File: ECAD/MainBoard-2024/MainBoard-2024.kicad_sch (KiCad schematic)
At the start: 67 parts, among them J1 XT60, J10 Conn_01x14, J11 Conn_01x03, J12 Conn_01x04, J13 Conn_01x03, J14 Conn_01x03, J16 XT30, J17 XT30, J2 Conn_01x04, J20 BAU, J21 BAU, J22 Conn_01x04, J23 Conn_01x02, J26 BAU, J27 BAU, J28 Conn_01x02, J29 Conn_01x02, J3 ConStep1, J30 Conn_01x03, J5 ConStep1, J6 ConStep1, J7 XT30, J8 Conn_01x02, J9 XT60, K1 CB1-P-24V, U1 Teensy3.5_All_Pins, U2 R-78B3.3-2.0, U3 PCA9685PW, U4 R-78B5.0-2.0

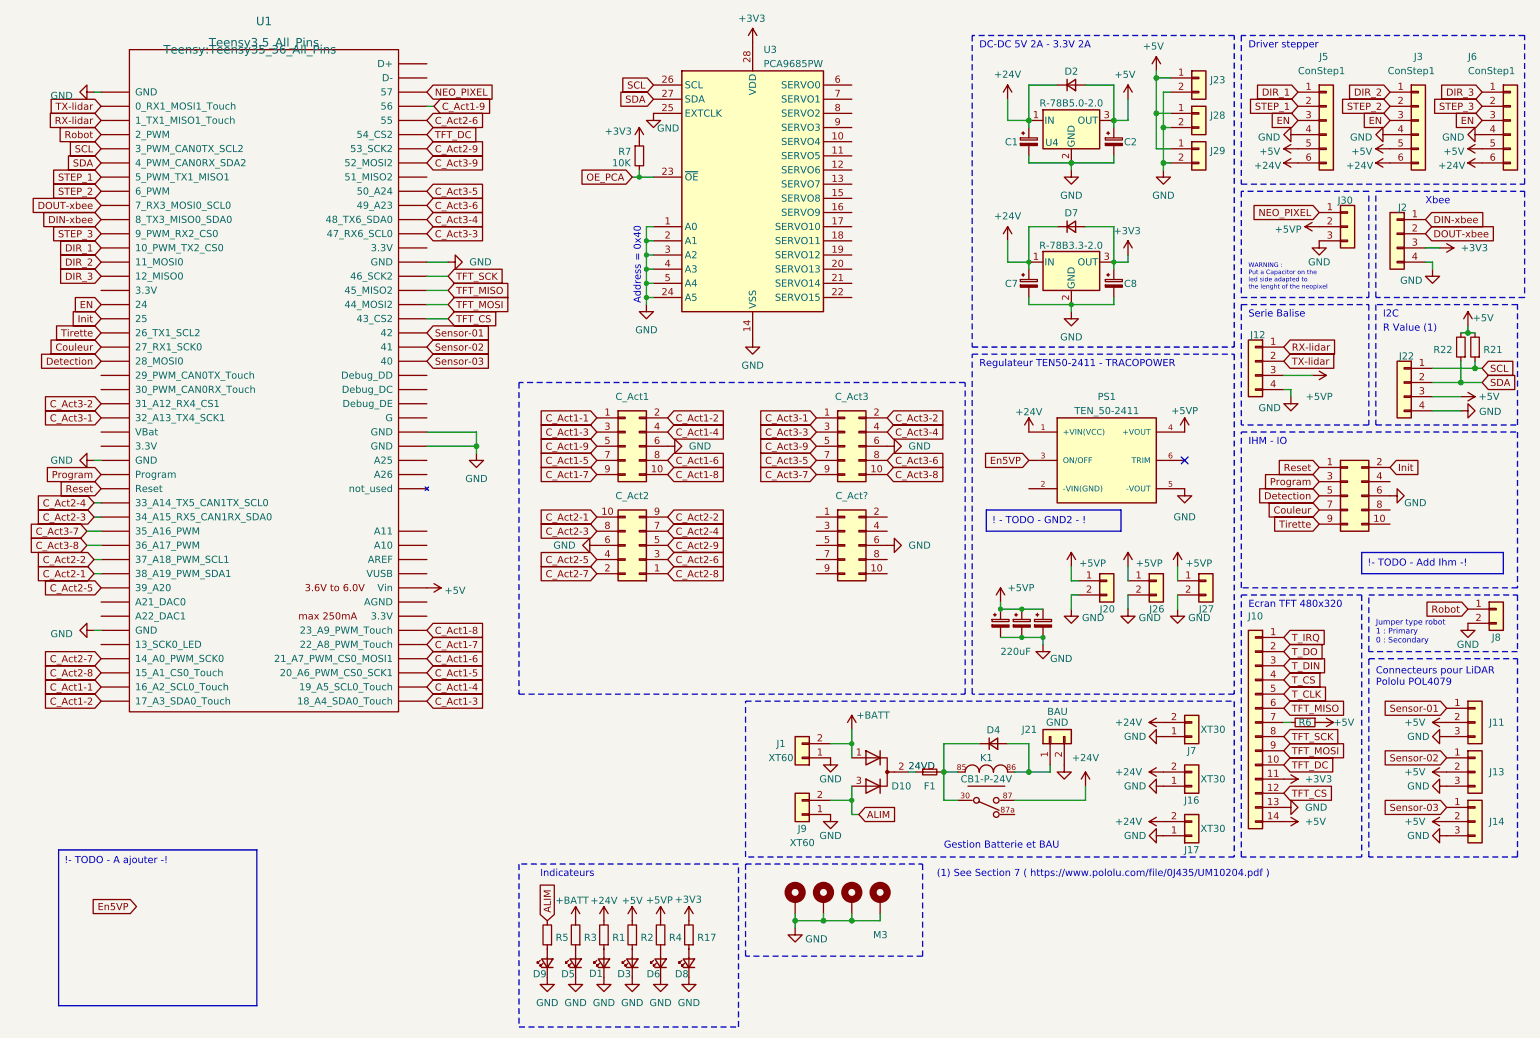
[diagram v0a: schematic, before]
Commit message: update component and edge cut
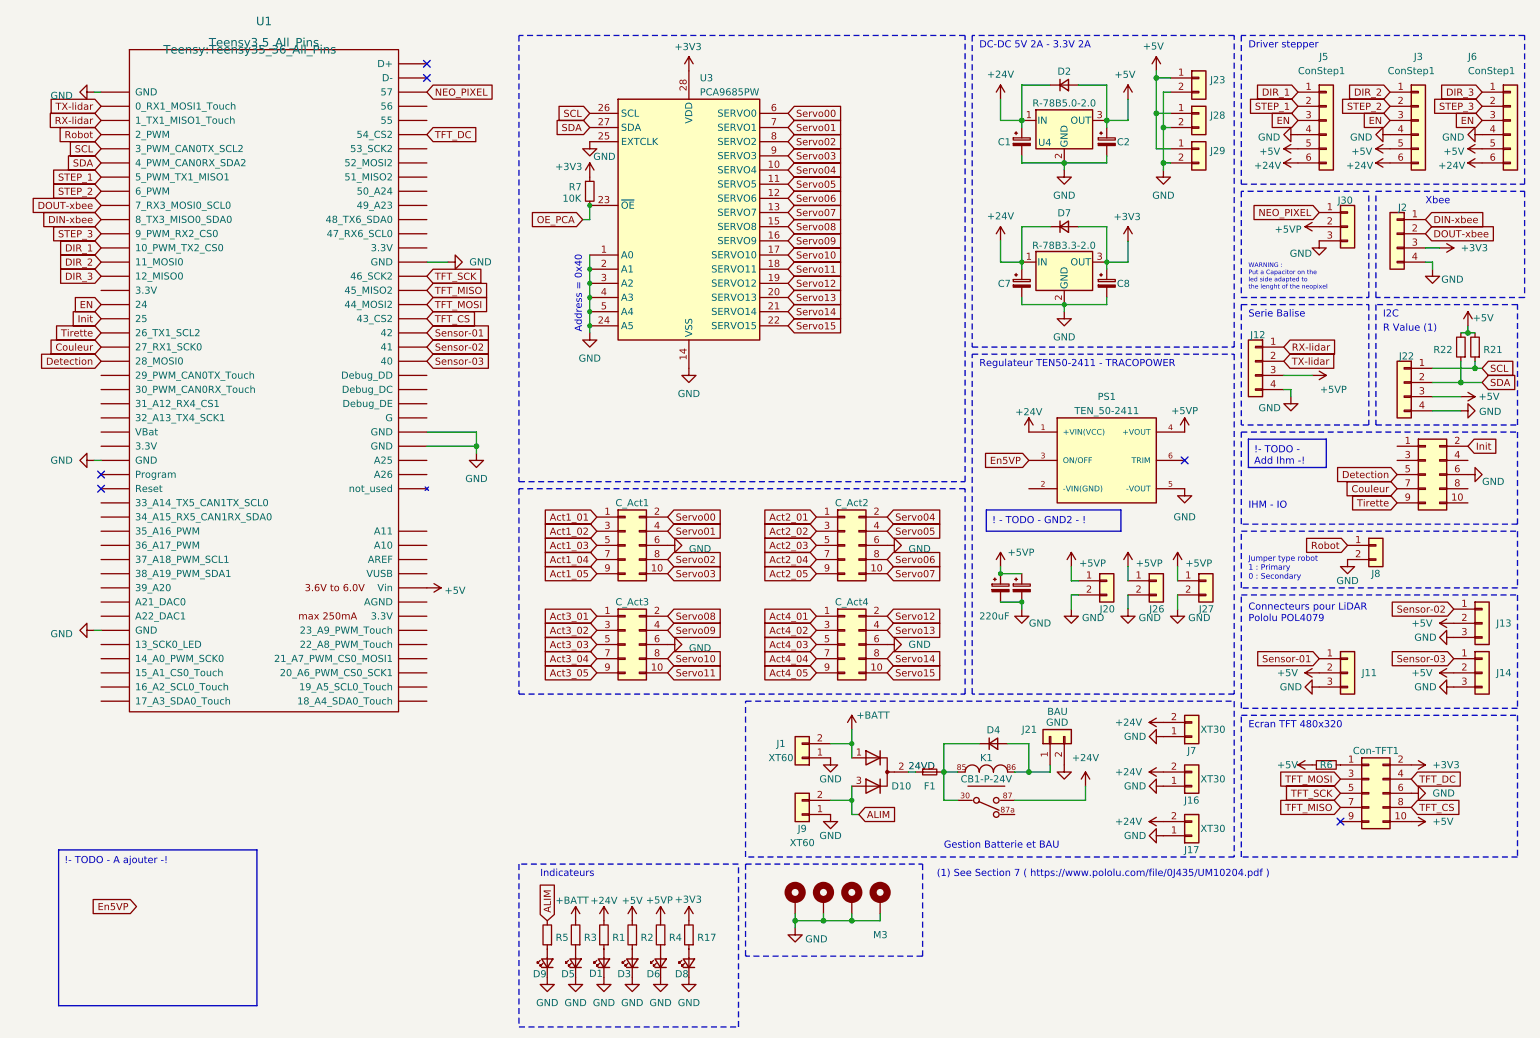
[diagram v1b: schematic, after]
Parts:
- removed C3: 220uF, Capacitor_THT:CP_Radial_D8.0mm_P3.80mm, symbol Device:CP_Small
- removed J10: Conn_01x14, Connector_PinSocket_2.54mm:PinSocket_1x14_P2.54mm_Vertical, symbol Connector_Generic:Conn_01x14
- added Con-TFT1: Conn_02x05_Odd_Even, Connector_IDC:IDC-Header_2x05_P2.54mm_Vertical, symbol Connector_Generic:Conn_02x05_Odd_Even
- gave numbers to parts that had none: 1
- renumbered C_Act3 to C_Act2, C_Act2 to C_Act3, C_Act4 to IHM-IO1
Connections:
- net +3V3: now also Con-TFT1.2 (Pin_2)
- net +5V: now also Con-TFT1.10 (Pin_10)
- net GND: now also Con-TFT1.6 (Pin_6)
- net TFT_CS: now also Con-TFT1.8 (Pin_8)
- net TFT_DC: now also Con-TFT1.4 (Pin_4)
- net TFT_MISO: now also Con-TFT1.7 (Pin_7)
- net TFT_MOSI: now also Con-TFT1.3 (Pin_3)
- net TFT_SCK: now also Con-TFT1.5 (Pin_5)
- net Servo04: now reaches U3.10 (SERVO4)
- net Servo04: now also C_Act2.2 (Pin_2)
- net Servo05: now reaches U3.11 (SERVO5)
- net Servo05: now also C_Act2.4 (Pin_4)
- net Servo06: now reaches U3.12 (SERVO6)
- net Servo06: now also C_Act2.8 (Pin_8)
- net Servo07: now reaches U3.13 (SERVO7)
- net Servo07: now also C_Act2.10 (Pin_10)
- net Servo08: now reaches U3.15 (SERVO8)
- net Servo08: now also C_Act3.2 (Pin_2)
- net Servo09: now reaches U3.16 (SERVO9)
- net Servo09: now also C_Act3.4 (Pin_4)
- net Servo10: now reaches U3.17 (SERVO10)
- net Servo10: now also C_Act3.8 (Pin_8)
- net Servo11: now reaches U3.18 (SERVO11)
- net Servo11: now also C_Act3.10 (Pin_10)
- net Servo12: now reaches U3.19 (SERVO12)
- net Servo12: now also C_Act4.2 (Pin_2)
- net Servo13: now reaches U3.20 (SERVO13)
- net Servo13: now also C_Act4.4 (Pin_4)
- net Servo14: now reaches U3.21 (SERVO14)
- net Servo14: now also C_Act4.8 (Pin_8)
- net Servo15: now reaches U3.22 (SERVO15)
- net Servo15: now also C_Act4.10 (Pin_10)
- net Servo00: now reaches U3.6 (SERVO0)
- net Servo00: now also C_Act1.2 (Pin_2)
- net Servo01: now reaches U3.7 (SERVO1)
- net Servo01: now also C_Act1.4 (Pin_4)
- net Servo02: now reaches U3.8 (SERVO2)
- net Servo02: now also C_Act1.8 (Pin_8)
- net Servo03: now reaches U3.9 (SERVO3)
- net Servo03: now also C_Act1.10 (Pin_10)
- net Act4_01: now reaches C_Act4.1 (Pin_1)
- net Act4_02: now reaches C_Act4.3 (Pin_3)
- net Act4_03: now reaches C_Act4.5 (Pin_5)
- net Act4_04: now reaches C_Act4.7 (Pin_7)
- net Act4_05: now reaches C_Act4.9 (Pin_9)
- net at R6.2: now also Con-TFT1.1 (Pin_1)
- net C_Act1-1: no longer names the net of U1.43 (16_A2_SCL0_Touch)
- net C_Act1-1: no longer C_Act1.1 (Pin_1)
- net C_Act1-2: no longer names the net of U1.44 (17_A3_SDA0_Touch)
- net C_Act1-2: no longer C_Act1.2 (Pin_2)
- net C_Act1-3: no longer names the net of U1.45 (18_A4_SDA0_Touch)
- net C_Act1-3: no longer C_Act1.3 (Pin_3)
- net C_Act1-4: no longer names the net of U1.46 (19_A5_SCL0_Touch)
- net C_Act1-4: no longer C_Act1.4 (Pin_4)
- net C_Act1-5: no longer names the net of U1.47 (20_A6_PWM_CS0_SCK1)
- net C_Act1-5: no longer C_Act1.7 (Pin_7)
- net C_Act1-6: no longer names the net of U1.48 (21_A7_PWM_CS0_MOSI1)
- net C_Act1-6: no longer C_Act1.8 (Pin_8)
- net C_Act1-7: no longer names the net of U1.49 (22_A8_PWM_Touch)
- net C_Act1-7: no longer C_Act1.9 (Pin_9)
- net C_Act1-8: no longer names the net of U1.50 (23_A9_PWM_Touch)
- net C_Act1-8: no longer C_Act1.10 (Pin_10)
- net C_Act1-9: no longer names the net of U1.85 (56)
- net C_Act1-9: no longer C_Act1.5 (Pin_5)
- net C_Act2-1: no longer names the net of U1.35 (38_A19_PWM_SDA1)
- net C_Act2-1: no longer C_Act3.10 (Pin_10)
- net C_Act2-2: no longer names the net of U1.34 (37_A18_PWM_SCL1)
- net C_Act2-2: no longer C_Act3.9 (Pin_9)
- net C_Act2-3: no longer names the net of U1.31 (34_A15_RX5_CAN1RX_SDA0)
- net C_Act2-3: no longer C_Act3.8 (Pin_8)
- net C_Act2-4: no longer names the net of U1.30 (33_A14_TX5_CAN1TX_SCL0)
- net C_Act2-4: no longer C_Act3.7 (Pin_7)
- net C_Act2-5: no longer names the net of U1.36 (39_A20)
- net C_Act2-5: no longer C_Act3.4 (Pin_4)
- net C_Act2-6: no longer names the net of U1.84 (55)
- net C_Act2-6: no longer C_Act3.3 (Pin_3)
- net C_Act2-7: no longer names the net of U1.41 (14_A0_PWM_SCK0)
- net C_Act2-7: no longer C_Act3.2 (Pin_2)
- net C_Act2-8: no longer names the net of U1.42 (15_A1_CS0_Touch)
- net C_Act2-8: no longer C_Act3.1 (Pin_1)
- net C_Act2-9: no longer names the net of U1.82 (53_SCK2)
- net C_Act2-9: no longer C_Act3.5 (Pin_5)
- net C_Act3-1: no longer names the net of U1.24 (32_A13_TX4_SCK1)
- net C_Act3-1: no longer C_Act2.1 (Pin_1)
- net C_Act3-2: no longer names the net of U1.23 (31_A12_RX4_CS1)
- net C_Act3-2: no longer C_Act2.2 (Pin_2)
- net C_Act3-3: no longer names the net of U1.76 (47_RX6_SCL0)
- net C_Act3-3: no longer C_Act2.3 (Pin_3)
- net C_Act3-4: no longer names the net of U1.77 (48_TX6_SDA0)
- net C_Act3-4: no longer C_Act2.4 (Pin_4)
- net C_Act3-5: no longer names the net of U1.79 (50_A24)
- net C_Act3-5: no longer C_Act2.7 (Pin_7)
- net C_Act3-6: no longer names the net of U1.78 (49_A23)
- net C_Act3-6: no longer C_Act2.8 (Pin_8)
- net C_Act3-7: no longer names the net of U1.32 (35_A16_PWM)
- net C_Act3-7: no longer C_Act2.9 (Pin_9)
- net C_Act3-8: no longer names the net of U1.33 (36_A17_PWM)
- net C_Act3-8: no longer C_Act2.10 (Pin_10)
- net C_Act3-9: no longer names the net of U1.81 (52_MOSI2)
- net C_Act3-9: no longer C_Act2.5 (Pin_5)
- net Program: no longer names the net of IHM-IO1.3 (Pin_3)
- net Program: no longer U1.28 (Program)
- net Reset: no longer names the net of IHM-IO1.1 (Pin_1)
- net Reset: no longer U1.29 (Reset)
- new net Act1_01: C_Act1.1 (Pin_1)
- new net Act1_02: C_Act1.3 (Pin_3)
- new net Act1_03: C_Act1.5 (Pin_5)
- new net Act1_04: C_Act1.7 (Pin_7)
- new net Act1_05: C_Act1.9 (Pin_9)
- new net Act2_01: C_Act2.1 (Pin_1)
- new net Act2_02: C_Act2.3 (Pin_3)
- new net Act2_03: C_Act2.5 (Pin_5)
- new net Act2_04: C_Act2.7 (Pin_7)
- new net Act2_05: C_Act2.9 (Pin_9)
- new net Act3_01: C_Act3.1 (Pin_1)
- new net Act3_02: C_Act3.3 (Pin_3)
- new net Act3_03: C_Act3.5 (Pin_5)
- new net Act3_04: C_Act3.7 (Pin_7)
- new net Act3_05: C_Act3.9 (Pin_9)
- no-connect marks 1 -> 6
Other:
- moved on the sheet: C1, C2, C7, C8, C_Act1, C_Act2, C_Act3, C_Act4, D2, D7, J11, J13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

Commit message: Simplify + add 12V regul
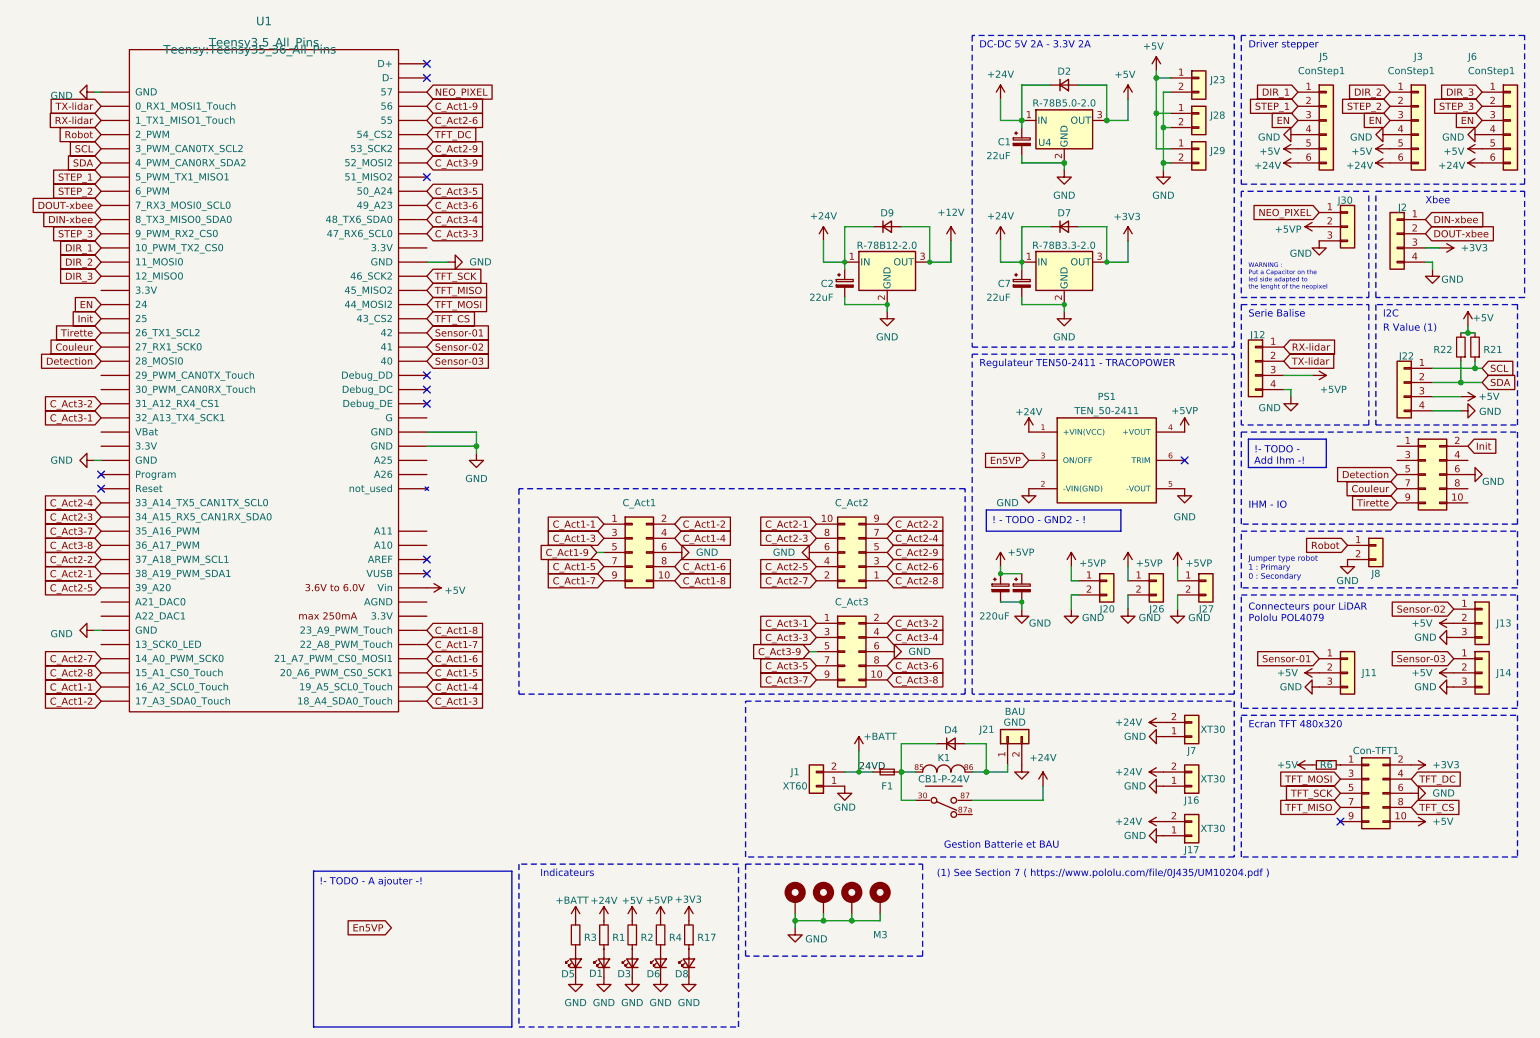
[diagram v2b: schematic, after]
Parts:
- removed C8: CP_Small, Capacitor_SMD:CP_Elec_5x5.4, symbol Device:CP_Small
- removed C_Act4: Conn_02x05_Odd_Even, Connector_IDC:IDC-Header_2x05_P2.54mm_Vertical, symbol Connector_Generic:Conn_02x05_Odd_Even
- removed D10: D_Dual_CommonCathode_AKA_Parallel, byv34-400:BYV34-400, symbol Device:D_Dual_CommonCathode_AKA_Parallel
- removed D9: LED_Small, LED_SMD:LED_1206_3216Metric_Pad1.42x1.75mm_HandSolder, symbol Device:LED_Small
- removed J9: XT60, Connector_AMASS:AMASS_XT60-M_1x02_P7.20mm_Vertical, symbol Connector_Generic:Conn_01x02
- removed R5: R_Small, Resistor_SMD:R_1206_3216Metric_Pad1.30x1.75mm_HandSolder, symbol Device:R_Small
- removed R7: 10K, Resistor_SMD:R_1206_3216Metric_Pad1.30x1.75mm_HandSolder, symbol Device:R_Small
- removed U3: PCA9685PW, Package_SO:TSSOP-28_4.4x9.7mm_P0.65mm, symbol Driver_LED:PCA9685PW
- added D9: D_Small, Diode_SMD:D_SMA_Handsoldering, symbol Device:D_Small
- added U3: R-78B12-2.0, Converter_DCDC:Converter_DCDC_RECOM_R-78E-0.5_THT, symbol Regulator_Switching:R-78B3.3-2.0
- C1, C2, C7: value CP_Small -> 22uF
- U2, U4: footprint Converter_DCDC:Converter_DCDC_RECOM_R-78B-2.0_THT -> Converter_DCDC:Converter_DCDC_RECOM_R-78E-0.5_THT
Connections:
- net 24VD is gone; now on net +BATT: F1.1
- net Act1_01 is gone; now on net C_Act1-1: C_Act1.1 (Pin_1)
- net Act1_02 is gone; now on net C_Act1-3: C_Act1.3 (Pin_3)
- net Act1_03 is gone; now on net C_Act1-9: C_Act1.5 (Pin_5)
- net Act1_04 is gone; now on net C_Act1-5: C_Act1.7 (Pin_7)
- net Act1_05 is gone; now on net C_Act1-7: C_Act1.9 (Pin_9)
- net Act2_01 is gone; now on net C_Act2-8: C_Act2.1 (Pin_1)
- net Act2_02 is gone; now on net C_Act2-6: C_Act2.3 (Pin_3)
- net Act2_03 is gone; now on net C_Act2-9: C_Act2.5 (Pin_5)
- net Act2_04 is gone; now on net C_Act2-4: C_Act2.7 (Pin_7)
- net Act2_05 is gone; now on net C_Act2-2: C_Act2.9 (Pin_9)
- net Act3_01 is gone; now on net C_Act3-1: C_Act3.1 (Pin_1)
- net Act3_02 is gone; now on net C_Act3-3: C_Act3.3 (Pin_3)
- net Act3_03 is gone; now on net C_Act3-9: C_Act3.5 (Pin_5)
- net Act3_04 is gone; now on net C_Act3-5: C_Act3.7 (Pin_7)
- net Act3_05 is gone; now on net C_Act3-7: C_Act3.9 (Pin_9)
- net Servo00 is gone; now on net C_Act1-2: C_Act1.2 (Pin_2)
- net Servo01 is gone; now on net C_Act1-4: C_Act1.4 (Pin_4)
- net Servo02 is gone; now on net C_Act1-6: C_Act1.8 (Pin_8)
- net Servo03 is gone; now on net C_Act1-8: C_Act1.10 (Pin_10)
- net Servo04 is gone; now on net C_Act2-7: C_Act2.2 (Pin_2)
- net Servo05 is gone; now on net C_Act2-5: C_Act2.4 (Pin_4)
- net Servo06 is gone; now on net C_Act2-3: C_Act2.8 (Pin_8)
- net Servo07 is gone; now on net C_Act2-1: C_Act2.10 (Pin_10)
- net Servo08 is gone; now on net C_Act3-2: C_Act3.2 (Pin_2)
- net Servo09 is gone; now on net C_Act3-4: C_Act3.4 (Pin_4)
- net Servo10 is gone; now on net C_Act3-6: C_Act3.8 (Pin_8)
- net Servo11 is gone; now on net C_Act3-8: C_Act3.10 (Pin_10)
- net +24V: now also C2.1, D9.1 (K), U3.1 (IN)
- net +5V: no longer C2.1
- net GND: now also PS1.2 (-VIN(GND)), U3.2 (GND)
- net C_Act3-2: now reaches U1.23 (31_A12_RX4_CS1)
- net C_Act3-1: now reaches U1.24 (32_A13_TX4_SCK1)
- net C_Act2-4: now reaches U1.30 (33_A14_TX5_CAN1TX_SCL0)
- net C_Act2-3: now reaches U1.31 (34_A15_RX5_CAN1RX_SDA0)
- net C_Act3-7: now reaches U1.32 (35_A16_PWM)
- net C_Act3-8: now reaches U1.33 (36_A17_PWM)
- net C_Act2-2: now reaches U1.34 (37_A18_PWM_SCL1)
- net C_Act2-1: now reaches U1.35 (38_A19_PWM_SDA1)
- net C_Act2-5: now reaches U1.36 (39_A20)
- net C_Act2-7: now reaches U1.41 (14_A0_PWM_SCK0)
- net C_Act2-8: now reaches U1.42 (15_A1_CS0_Touch)
- net C_Act1-1: now reaches U1.43 (16_A2_SCL0_Touch)
- net C_Act1-2: now reaches U1.44 (17_A3_SDA0_Touch)
- net C_Act1-3: now reaches U1.45 (18_A4_SDA0_Touch)
- net C_Act1-4: now reaches U1.46 (19_A5_SCL0_Touch)
- net C_Act1-5: now reaches U1.47 (20_A6_PWM_CS0_SCK1)
- net C_Act1-6: now reaches U1.48 (21_A7_PWM_CS0_MOSI1)
- net C_Act1-7: now reaches U1.49 (22_A8_PWM_Touch)
- net C_Act1-8: now reaches U1.50 (23_A9_PWM_Touch)
- net C_Act3-3: now reaches U1.76 (47_RX6_SCL0)
- net C_Act3-4: now reaches U1.77 (48_TX6_SDA0)
- net C_Act3-6: now reaches U1.78 (49_A23)
- net C_Act3-5: now reaches U1.79 (50_A24)
- net C_Act3-9: now reaches U1.81 (52_MOSI2)
- net C_Act2-9: now reaches U1.82 (53_SCK2)
- net C_Act2-6: now reaches U1.84 (55)
- net C_Act1-9: now reaches U1.85 (56)
- new net +12V: D9.2 (A), U3.3 (OUT)
- no-connect marks 6 -> 12
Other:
- note removed: "Address = 0x40"
- moved on the sheet: D4, F1, J1, J21, K1

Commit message: change relay
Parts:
- removed K1: CB1-P-24V, CB1-P-24V:Panasonic_Electric_Works-CB1-P-24V-MFG, symbol CB1-P-24V:CB1-P-24V
- added K2: FINDER-36.11, Relay_THT:Relay_SPDT_Finder_36.11, symbol Relay:FINDER-36.11
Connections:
- net +24V: now also K2.14
- net at D4.1 (K), F1.2: now also K2.11, K2.A2
- net at D4.2 (A), J21.1 (Pin_1): now also K2.A1
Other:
- moved on the sheet: D4
